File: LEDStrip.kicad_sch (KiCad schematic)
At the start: 4 parts, among them J301 WAGO-2065, J302 WAGO-2065, J303 WAGO-2065, U301 74AHC1G125

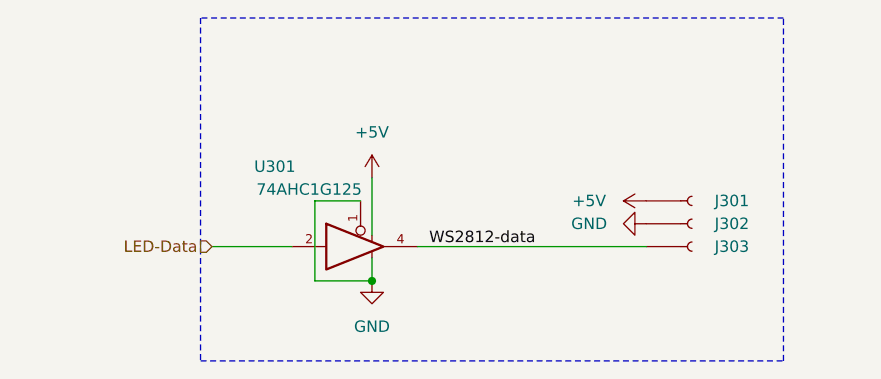
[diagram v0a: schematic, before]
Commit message: Replace Order_Number
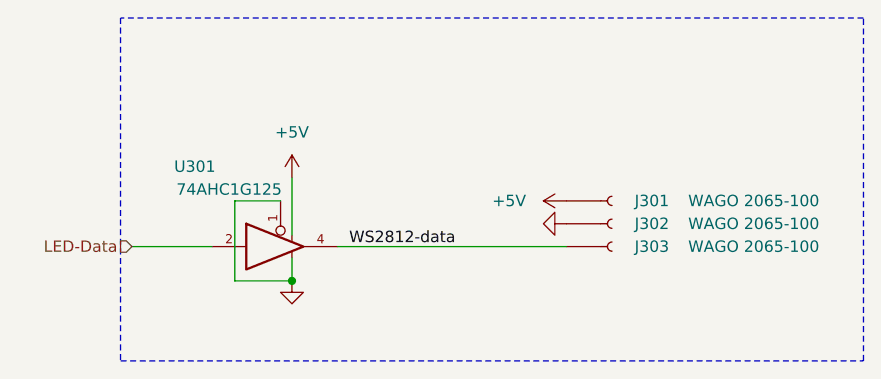
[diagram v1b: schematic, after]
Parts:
- J301, J302, J303: value WAGO-2065 -> WAGO 2065-100; Manufacturer (none) -> WAGO; Product (none) -> 2065-100/998-403
- U301: footprint Package_TO_SOT_SMD:SOT-23-5 -> V2_Package_TO_SOT_SMD:SOT-23-5; Manufacturer (none) -> Texas Instruments; Mouser (none) -> 595-SN74AHC1G125DBVR; Product (none) -> SN74AHC1G125DBVR
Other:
- moved on the sheet: J301, J302, J303, U301

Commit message: Replace diode
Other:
- title: LED Strip -> V2 control
